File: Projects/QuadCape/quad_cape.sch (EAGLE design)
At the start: 9 parts, among them U1 ADXL345, U2 ITG-3200, U3 LS20031, U4 ATMEGA8U2AU

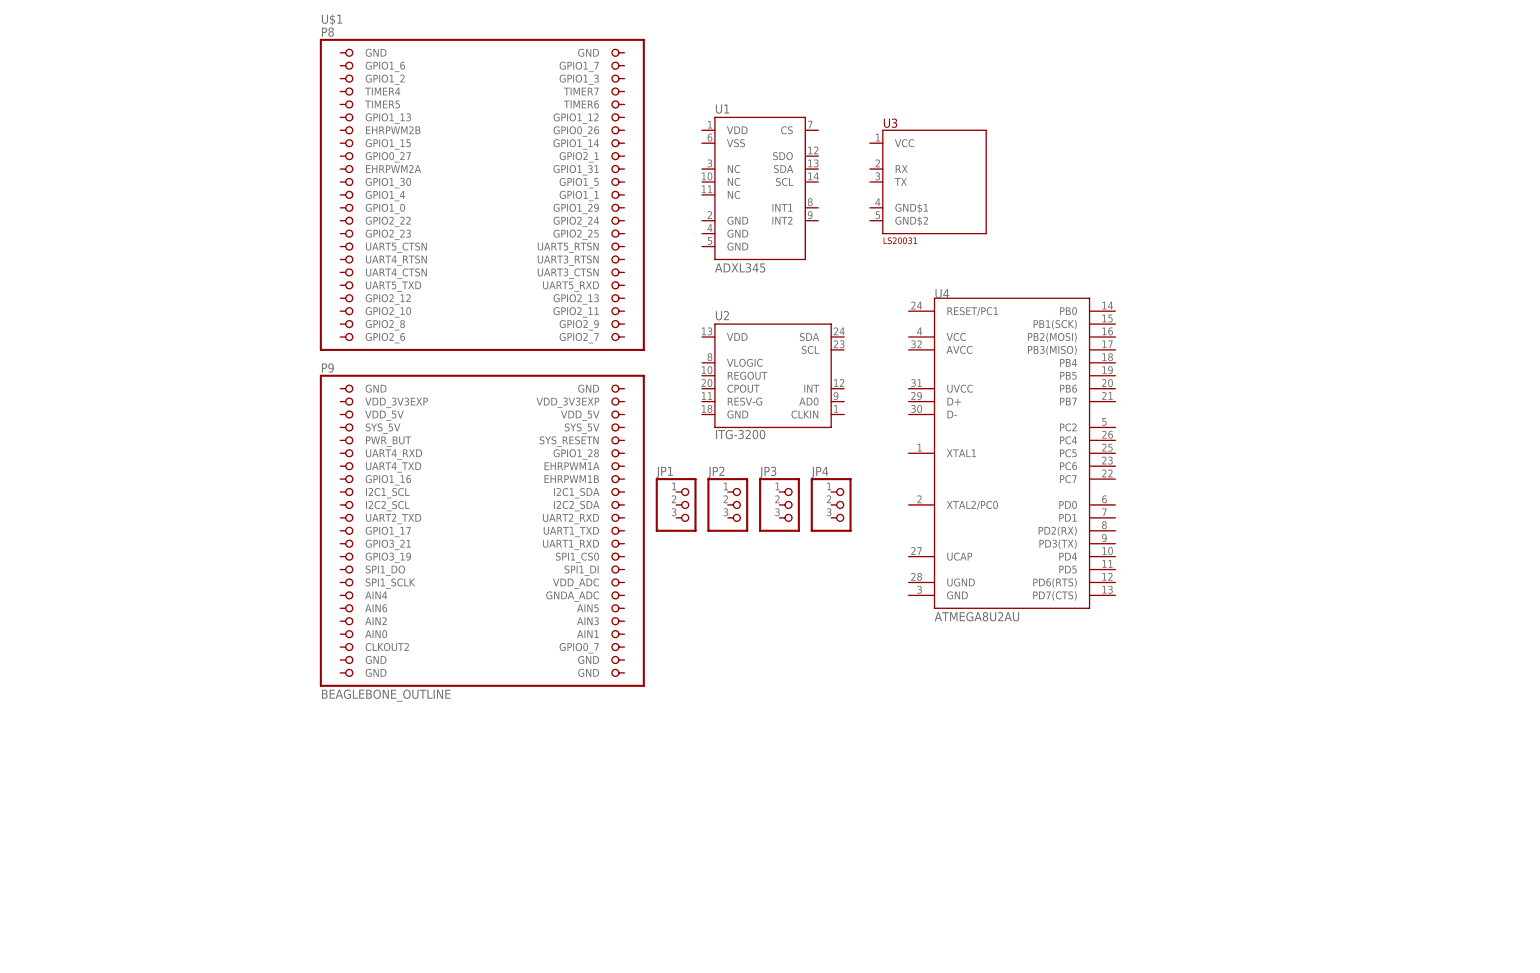
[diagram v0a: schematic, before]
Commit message: Began wiring up some connections
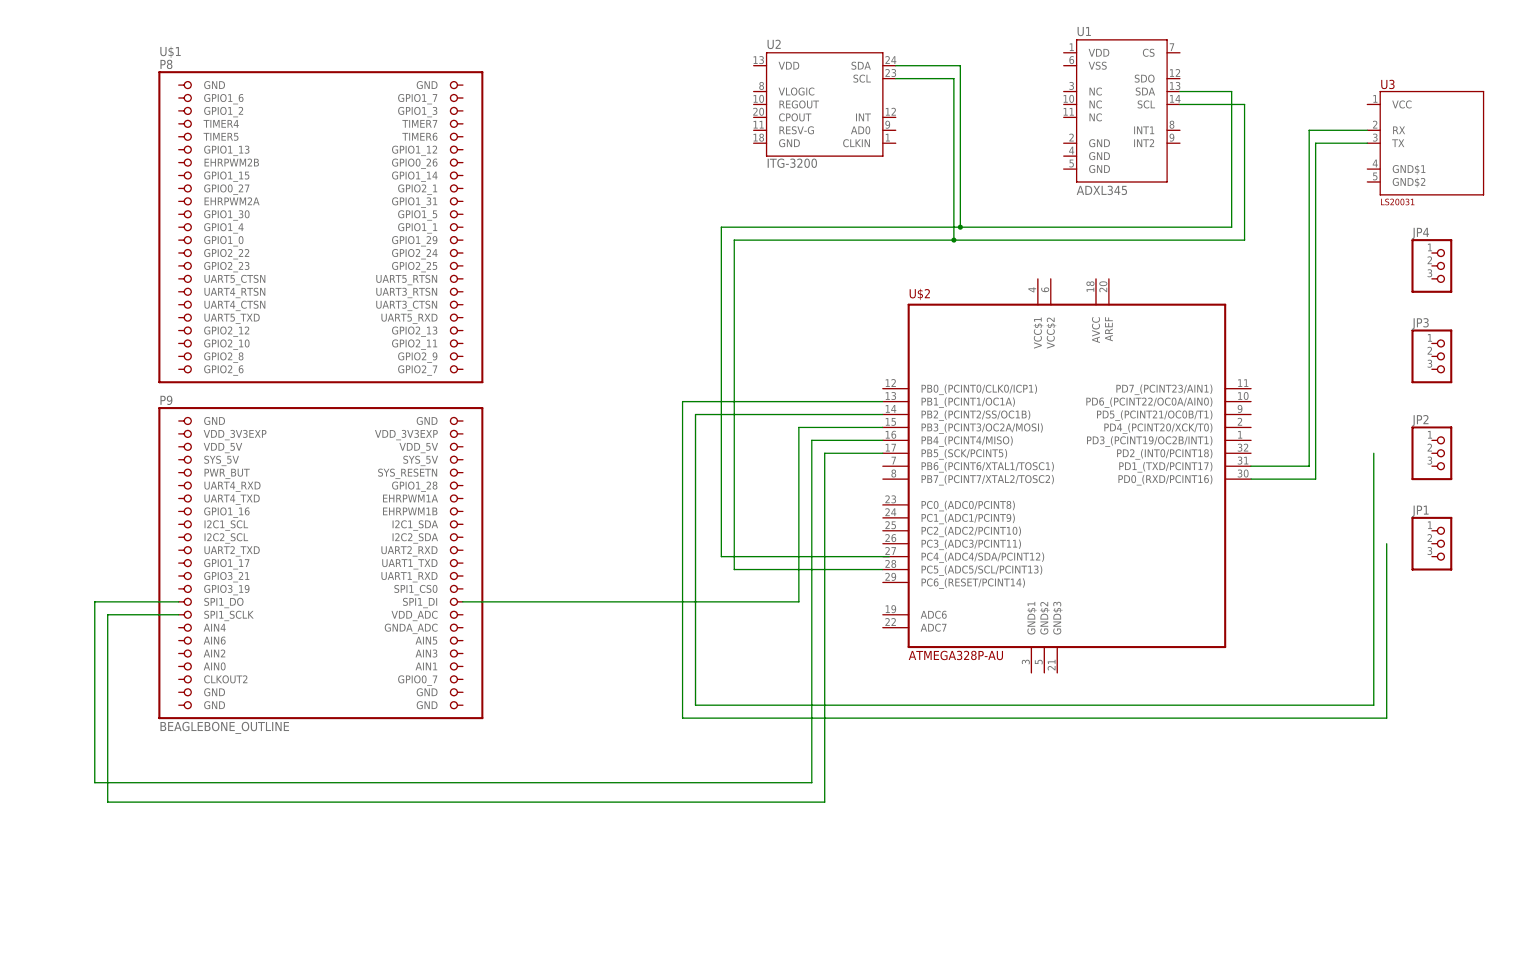
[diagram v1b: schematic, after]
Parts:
- removed U4: ATMEGA8U2AU, SparkFun-DigitalIC:ATMEGA8U2AU
- added U$2: ATMEGA328P-AU, custom:ATMEGA328P-AU
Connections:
- new net N$1: U$2.PD0_(RXD/PCINT16), U3.TX
- new net N$10: U$2.PB1_(PCINT1/OC1A)
- new net N$2: U$2.PD1_(TXD/PCINT17), U3.RX
- new net N$3: U$1.SPI1_DO, U$2.PB4_(PCINT4/MISO)
- new net N$4: U$1.SPI1_DI, U$2.PB3_(PCINT3/OC2A/MOSI)
- new net N$5: U$2.PB2_(PCINT2/SS/OC1B)
- new net N$6: U$1.SPI1_SCLK, U$2.PB5_(SCK/PCINT5)
- new net N$7: U1.SDA, U2.SDA
- new net N$8: U$2.PC5_(ADC5/SCL/PCINT13), U1.SCL, U2.SCL
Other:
- moved on the sheet: JP1, JP2, JP3, JP4, U$1, U1, U2, U3
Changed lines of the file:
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@@
 <setting verticaltext="up"/>
 </settings>
-<grid distance="0.1" unitdist="inch" unit="inch" style="lines" multiple="1" display="no" altdistance="0.01" altunitdist="inch" altunit="inch"/>
+<grid distance="0.05" unitdist="inch" unit="inch" style="lines" multiple="1" display="no" altdistance="0.01" altunitdist="inch" altunit="inch"/>
 <layers>
 <layer number="1" name="Top" color="4" fill="1" visible="no" active="no"/>
@@
 <part name="JP3" library="adafruit" deviceset="PINHD-1X3" device=""/>
 <part name="JP4" library="adafruit" deviceset="PINHD-1X3" device=""/>
-<part name="U4" library="SparkFun-DigitalIC" deviceset="ATMEGA8U2" device="AU"/>
+<part name="U$2" library="custom" deviceset="ATMEGA328P-AU" device=""/>
 </parts>
 <sheets>
@@
 </plain>
 <instances>
-<instance part="U$1" gate="G$1" x="17.78" y="30.48"/>
-<instance part="U1" gate="G$1" x="71.12" y="66.04"/>
-<instance part="U2" gate="G$1" x="73.66" y="27.94"/>
-<instance part="U3" gate="G$1" x="106.68" y="66.04"/>
-<instance part="JP1" gate="A" x="58.42" y="2.54"/>
-<instance part="JP2" gate="A" x="68.58" y="2.54"/>
-<instance part="JP3" gate="A" x="78.74" y="2.54"/>
-<instance part="JP4" gate="A" x="88.9" y="2.54"/>
-<instance part="U4" gate="G$1" x="121.92" y="12.7"/>
+<instance part="U$1" gate="G$1" x="-13.97" y="24.13"/>
+<instance part="U1" gate="G$1" x="142.24" y="81.28"/>
+<instance part="U2" gate="G$1" x="83.82" y="81.28"/>
+<instance part="U3" gate="G$1" x="204.47" y="73.66"/>
+<instance part="JP1" gate="A" x="207.01" y="-5.08"/>
+<instance part="JP2" gate="A" x="207.01" y="12.7"/>
+<instance part="JP3" gate="A" x="207.01" y="31.75"/>
+<instance part="JP4" gate="A" x="207.01" y="49.53"/>
+<instance part="U$2" gate="G$1" x="134.62" y="5.08"/>
 </instances>
 <busses>
 </busses>
 <nets>
+<net name="N$1" class="0">
+<segment>
+<pinref part="U3" gate="G$1" pin="TX"/>
+<wire x1="191.77" y1="73.66" x2="181.61" y2="73.66" width="0.1524" layer="91"/>
+<wire x1="181.61" y1="73.66" x2="181.61" y2="7.62" width="0.1524" layer="91"/>
+<pinref part="U$2" gate="G$1" pin="PD0_(RXD/PCINT16)"/>
+<wire x1="181.61" y1="7.62" x2="168.91" y2="7.62" width="0.1524" layer="91"/>
+</segment>
+</net>
+<net name="N$2" class="0">
+<segment>
+<pinref part="U3" gate="G$1" pin="RX"/>
+<wire x1="191.77" y1="76.2" x2="180.34" y2="76.2" width="0.1524" layer="91"/>
+<wire x1="180.34" y1="76.2" x2="180.34" y2="10.16" width="0.1524" layer="91"/>
+<pinref part="U$2" gate="G$1" pin="PD1_(TXD/PCINT17)"/>
+<wire x1="180.34" y1="10.16" x2="168.91" y2="10.16" width="0.1524" layer="91"/>
+</segment>
+</net>
+<net name="N$3" class="0">
+<segment>
+<pinref part="U$1" gate="G$1" pin="SPI1_DO"/>
+<wire x1="-41.91" y1="-16.51" x2="-58.42" y2="-16.51" width="0.1524" layer="91"/>
+<wire x1="-58.42" y1="-16.51" x2="-58.42" y2="-52.07" width="0.1524" layer="91"/>
+<wire x1="-58.42" y1="-52.07" x2="82.55" y2="-52.07" width="0.1524" layer="91"/>
+<wire x1="82.55" y1="-52.07" x2="82.55" y2="15.24" width="0.1524" layer="91"/>
+<pinref part="U$2" gate="G$1" pin="PB4_(PCINT4/MISO)"/>
+<wire x1="82.55" y1="15.24" x2="96.52" y2="15.24" width="0.1524" layer="91"/>
+</segment>
+</net>
+<net name="N$4" class="0">
+<segment>
+<pinref part="U$1" gate="G$1" pin="SPI1_DI"/>
+<wire x1="13.97" y1="-16.51" x2="80.01" y2="-16.51" width="0.1524" layer="91"/>
+<pinref part="U$2" gate="G$1" pin="PB3_(PCINT3/OC2A/MOSI)"/>
+<wire x1="80.01" y1="-16.51" x2="80.01" y2="17.78" width="0.1524" layer="91"/>
+<wire x1="80.01" y1="17.78" x2="96.52" y2="17.78" width="0.1524" layer="91"/>
+</segment>
+</net>
+<net name="N$6" class="0">
+<segment>
+<pinref part="U$2" gate="G$1" pin="PB5_(SCK/PCINT5)"/>
+<wire x1="96.52" y1="12.7" x2="85.09" y2="12.7" width="0.1524" layer="91"/>
+<wire x1="85.09" y1="12.7" x2="85.09" y2="-55.88" width="0.1524" layer="91"/>
+<wire x1="85.09" y1="-55.88" x2="-55.88" y2="-55.88" width="0.1524" layer="91"/>
+<wire x1="-55.88" y1="-55.88" x2="-55.88" y2="-19.05" width="0.1524" layer="91"/>
+<pinref part="U$1" gate="G$1" pin="SPI1_SCLK"/>
+<wire x1="-55.88" y1="-19.05" x2="-41.91" y2="-19.05" width="0.1524" layer="91"/>
+</segment>
+</net>
+<net name="N$7" class="0">
+<segment>
+<wire x1="97.79" y1="-7.62" x2="64.77" y2="-7.62" width="0.1524" layer="91"/>
+<wire x1="64.77" y1="-7.62" x2="64.77" y2="57.15" width="0.1524" layer="91"/>
+<wire x1="64.77" y1="57.15" x2="111.76" y2="57.15" width="0.1524" layer="91"/>
+<pinref part="U2" gate="G$1" pin="SDA"/>
+<wire x1="111.76" y1="57.15" x2="165.1" y2="57.15" width="0.1524" layer="91"/>
+<wire x1="99.06" y1="88.9" x2="111.76" y2="88.9" width="0.1524" layer="91"/>
+<wire x1="111.76" y1="88.9" x2="111.76" y2="57.15" width="0.1524" layer="91"/>
+<junction x="111.76" y="57.15"/>
+<pinref part="U1" gate="G$1" pin="SDA"/>
+<wire x1="154.94" y1="83.82" x2="165.1" y2="83.82" width="0.1524" layer="91"/>
+<wire x1="165.1" y1="83.82" x2="165.1" y2="57.15" width="0.1524" layer="91"/>
+</segment>
+</net>
+<net name="N$8" class="0">
+<segment>
+<pinref part="U$2" gate="G$1" pin="PC5_(ADC5/SCL/PCINT13)"/>
+<wire x1="96.52" y1="-10.16" x2="67.31" y2="-10.16" width="0.1524" layer="91"/>
+<wire x1="67.31" y1="-10.16" x2="67.31" y2="54.61" width="0.1524" layer="91"/>
+<wire x1="67.31" y1="54.61" x2="110.49" y2="54.61" width="0.1524" layer="91"/>
+<pinref part="U2" gate="G$1" pin="SCL"/>
+<wire x1="110.49" y1="54.61" x2="167.64" y2="54.61" width="0.1524" layer="91"/>
+<wire x1="99.06" y1="86.36" x2="110.49" y2="86.36" width="0.1524" layer="91"/>
+<wire x1="110.49" y1="86.36" x2="110.49" y2="54.61" width="0.1524" layer="91"/>
+<junction x="110.49" y="54.61"/>
+<pinref part="U1" gate="G$1" pin="SCL"/>
+<wire x1="154.94" y1="81.28" x2="167.64" y2="81.28" width="0.1524" layer="91"/>
+<wire x1="167.64" y1="81.28" x2="167.64" y2="54.61" width="0.1524" layer="91"/>
+</segment>
+</net>
+<net name="N$10" class="0">
+<segment>
+<pinref part="U$2" gate="G$1" pin="PB1_(PCINT1/OC1A)"/>
+<wire x1="96.52" y1="22.86" x2="57.15" y2="22.86" width="0.1524" layer="91"/>
+<wire x1="57.15" y1="22.86" x2="57.15" y2="-39.37" width="0.1524" layer="91"/>
+<wire x1="57.15" y1="-39.37" x2="195.58" y2="-39.37" width="0.1524" layer="91"/>
+<wire x1="195.58" y1="-39.37" x2="195.58" y2="-5.08" width="0.1524" layer="91"/>
+</segment>
+</net>
+<net name="N$5" class="0">
+<segment>
+<pinref part="U$2" gate="G$1" pin="PB2_(PCINT2/SS/OC1B)"/>
+<wire x1="96.52" y1="20.32" x2="59.69" y2="20.32" width="0.1524" layer="91"/>
+<wire x1="59.69" y1="20.32" x2="59.69" y2="-36.83" width="0.1524" layer="91"/>
+<wire x1="59.69" y1="-36.83" x2="193.04" y2="-36.83" width="0.1524" layer="91"/>
+<wire x1="193.04" y1="-36.83" x2="193.04" y2="12.7" width="0.1524" layer="91"/>
+</segment>
+</net>
 </nets>
 </sheet>

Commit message: Swapped symbol for Mega328 for a better on I had already made a while ago (oops)
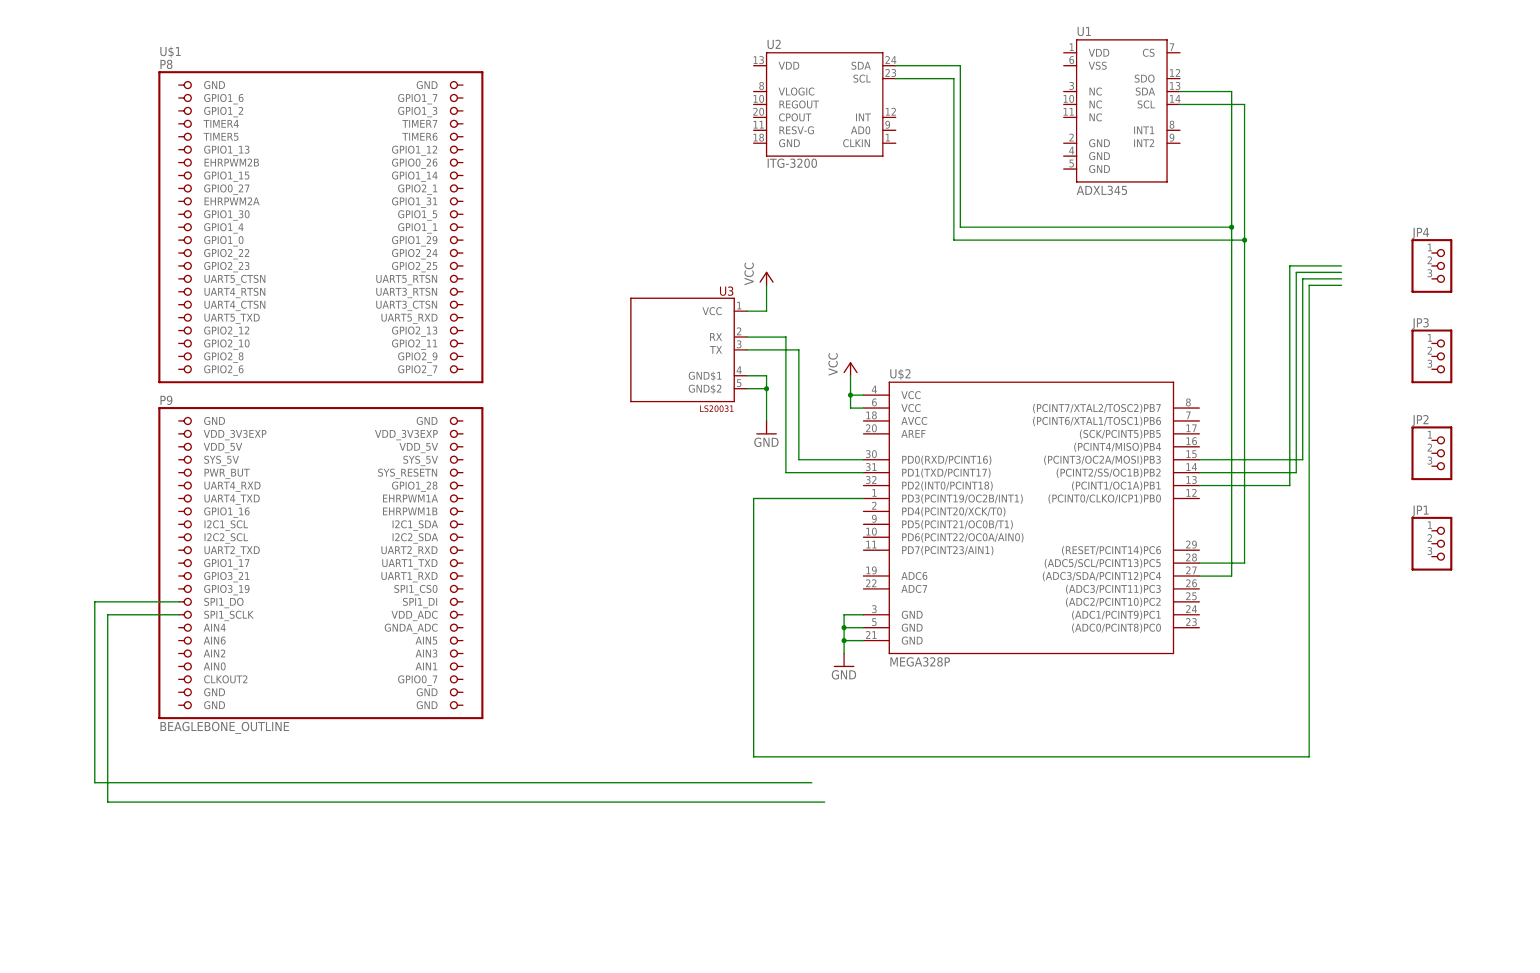
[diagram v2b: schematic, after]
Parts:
- U$2: value ATMEGA328P-AU -> MEGA328P; device custom:ATMEGA328P-AU -> custom:MEGA328P
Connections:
- removed net N$10: U$2.PB1_(PCINT1/OC1A)
- removed net N$5: U$2.PB2_(PCINT2/SS/OC1B)
- new net GND: U$2.GND@1, U$2.GND@2, U$2.GND@3, U3.GND$1, U3.GND$2
- new net N$11: U$2.(PCINT3/OC2A/MOSI)PB3
- new net N$12: U$2.PD3(PCINT19/OC2B/INT1)
- new net N$9: U$2.(PCINT2/SS/OC1B)PB2
- new net VCC: U$2.VCC@1, U$2.VCC@2, U3.VCC
- net N$1: now also U$2.PD0(RXD/PCINT16); no longer U$2.PD0_(RXD/PCINT16)
- net N$2: now also U$2.PD1(TXD/PCINT17); no longer U$2.PD1_(TXD/PCINT17)
- net N$3: no longer U$2.PB4_(PCINT4/MISO)
- net N$4: now also U$2.(PCINT1/OC1A)PB1; no longer U$1.SPI1_DI, U$2.PB3_(PCINT3/OC2A/MOSI)
- net N$6: no longer U$2.PB5_(SCK/PCINT5)
- net N$7: now also U$2.(ADC3/SDA/PCINT12)PC4
- net N$8: now also U$2.(ADC5/SCL/PCINT13)PC5; no longer U$2.PC5_(ADC5/SCL/PCINT13)
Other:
- moved on the sheet: U$2, U3

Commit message: Sync
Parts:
- JP1, JP2, JP3, JP4: device adafruit:PINHD-1X3 -> SparkFun-Connectors:M04PTH
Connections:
- new net +5V: JP1.1, JP2.1, JP3.1, JP4.1, U$1.VDD_5V@2
- new net N$15: U$1.SPI1_SCLK, U$2.(SCK/PCINT5)PB5
- new net N$5: JP3.2, U$2.PD6(PCINT22/OC0A/AIN0)
- net GND: now also JP1.3, JP1.4, JP2.3, JP2.4, JP3.3, JP3.4, JP4.3, JP4.4, U$1.GND@3, U$1.GND@4, U$1.GND@5, U$1.GND@6, U$1.GND@7, U1.GND@2, U1.GND@4, U1.GND@5, U2.GND
- net N$11: now also U$1.SPI1_CS0; no longer U$2.(PCINT3/OC2A/MOSI)PB3
- net N$12: now also JP4.2, U$2.PD5(PCINT21/OC0B/T1); no longer U$2.PD3(PCINT19/OC2B/INT1)
- net N$3: now also U$2.(PCINT3/OC2A/MOSI)PB3
- net N$4: now also JP2.2
- net N$6: now also U$1.SPI1_DI, U$2.(PCINT4/MISO)PB4; no longer U$1.SPI1_SCLK
- net N$9: now also JP1.2
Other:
- moved on the sheet: U3
